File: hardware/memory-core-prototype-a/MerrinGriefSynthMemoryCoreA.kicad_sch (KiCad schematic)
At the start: 0 parts

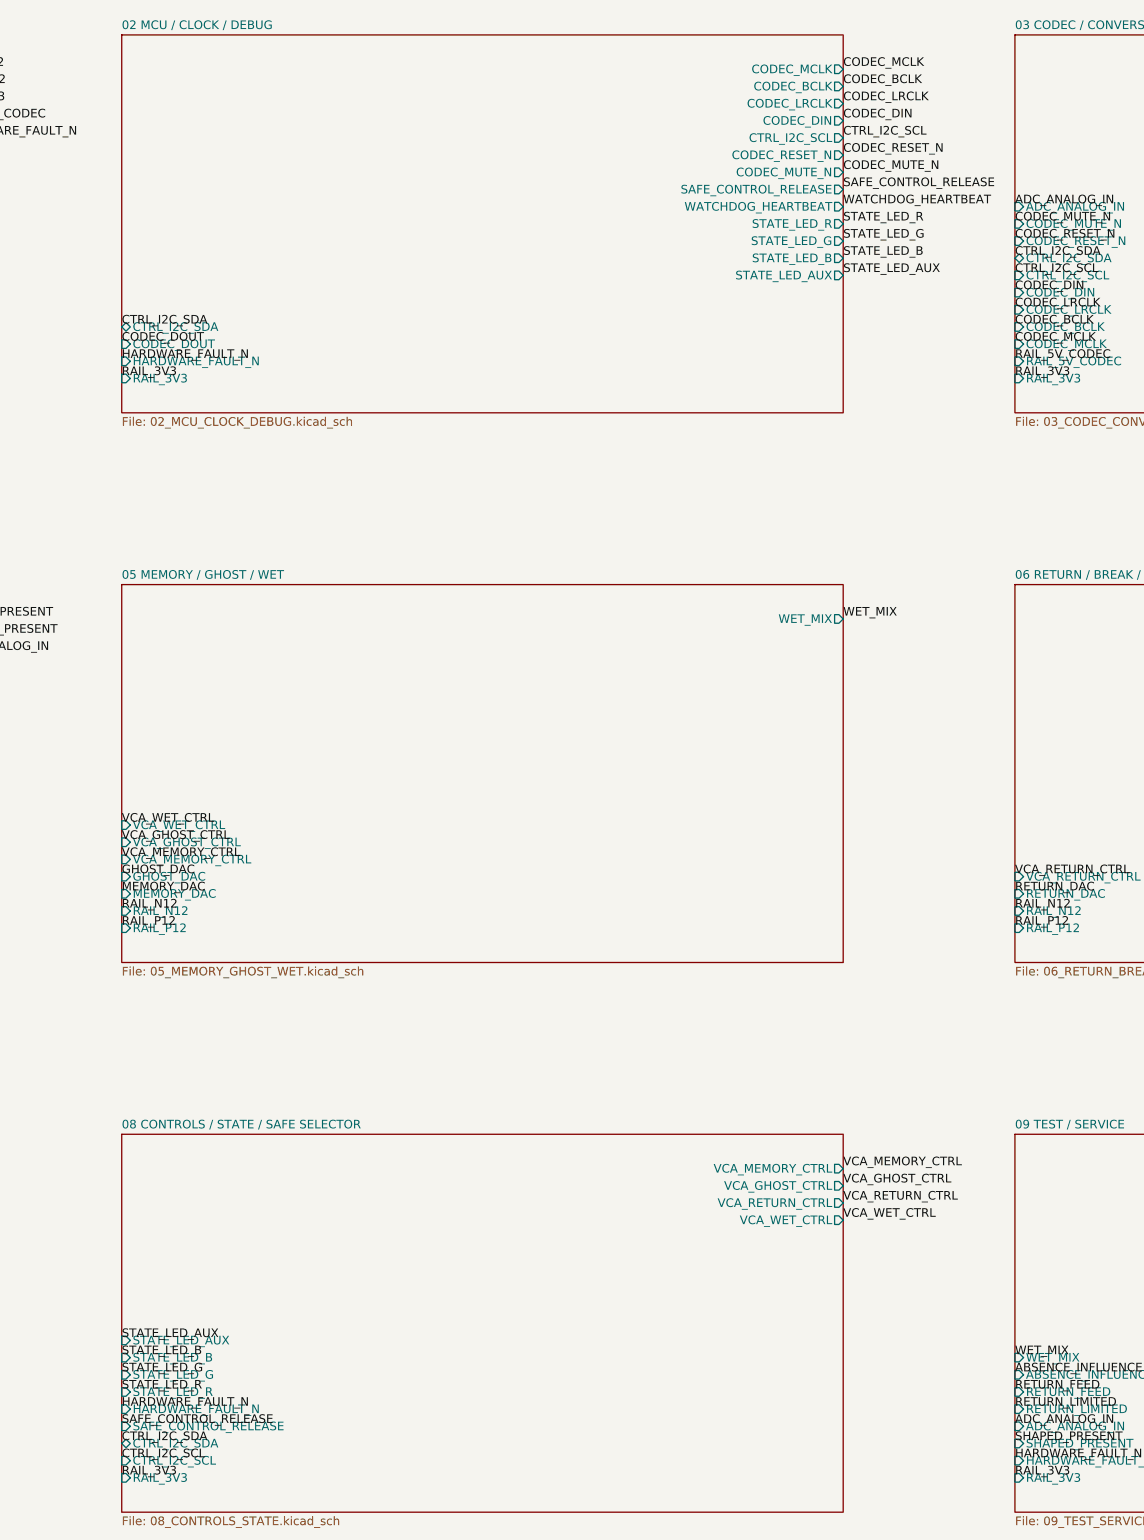
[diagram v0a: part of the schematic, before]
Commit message: Capture ERC-validated controls and state sheet
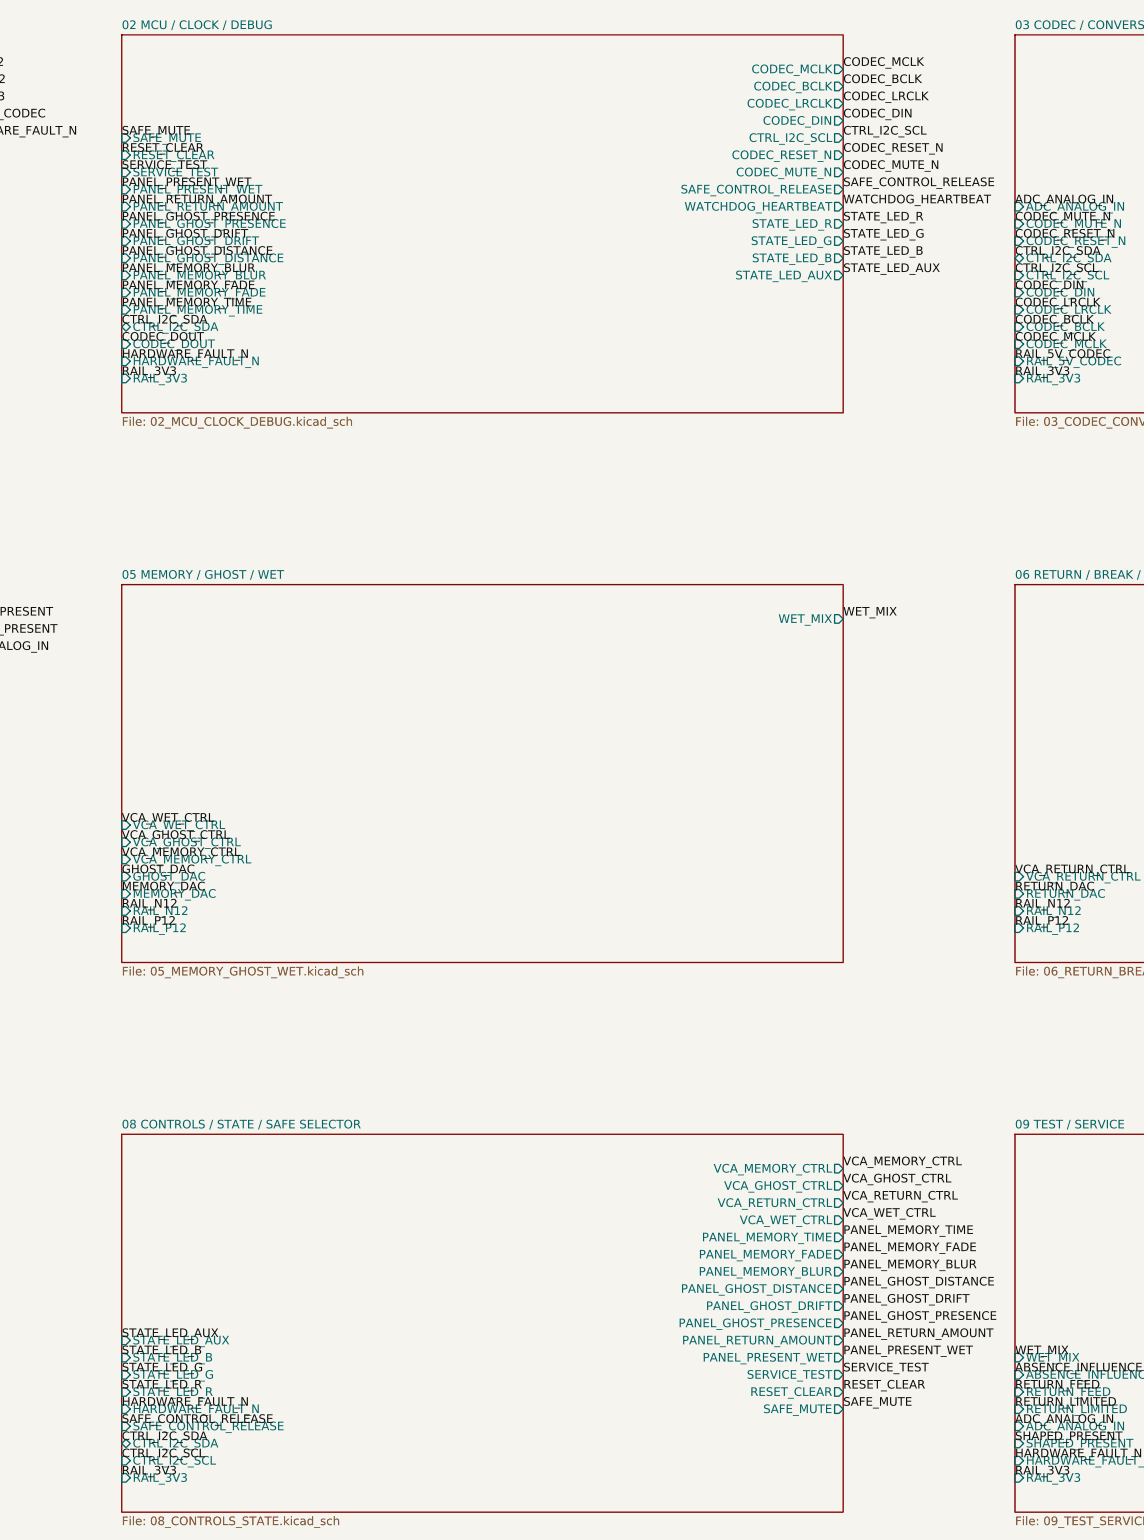
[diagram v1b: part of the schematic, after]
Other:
- sheet 02 MCU / CLOCK / DEBUG ports: added PANEL_GHOST_DISTANCE, PANEL_GHOST_DRIFT, PANEL_GHOST_PRESENCE, PANEL_MEMORY_BLUR, PANEL_MEMORY_FADE, PANEL_MEMORY_TIME, PANEL_PRESENT_WET, PANEL_RETURN_AMOUNT, RESET_CLEAR, SAFE_MUTE, SERVICE_TEST; removed none
- sheet 08 CONTROLS / STATE / SAFE SELECTOR ports: added PANEL_GHOST_DISTANCE, PANEL_GHOST_DRIFT, PANEL_GHOST_PRESENCE, PANEL_MEMORY_BLUR, PANEL_MEMORY_FADE, PANEL_MEMORY_TIME, PANEL_PRESENT_WET, PANEL_RETURN_AMOUNT, RESET_CLEAR, SAFE_MUTE, SERVICE_TEST; removed none

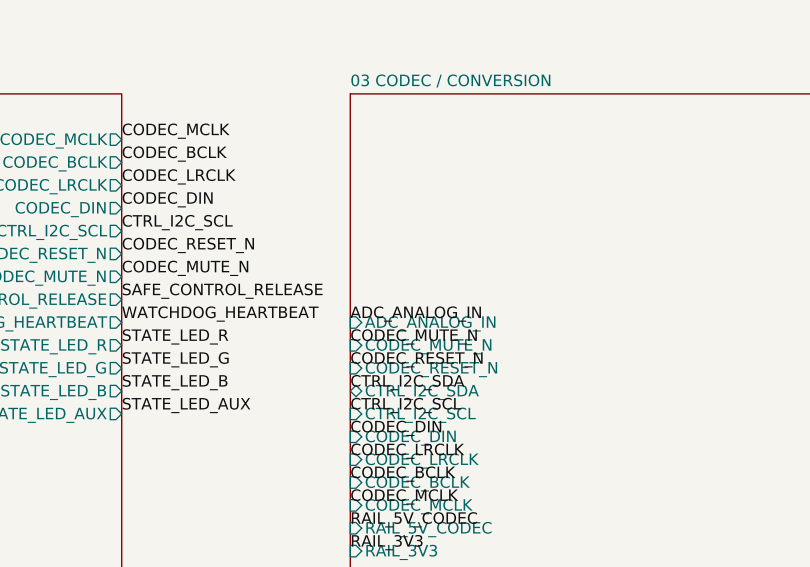
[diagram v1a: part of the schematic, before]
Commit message: Capture ERC-validated codec conversion sheet
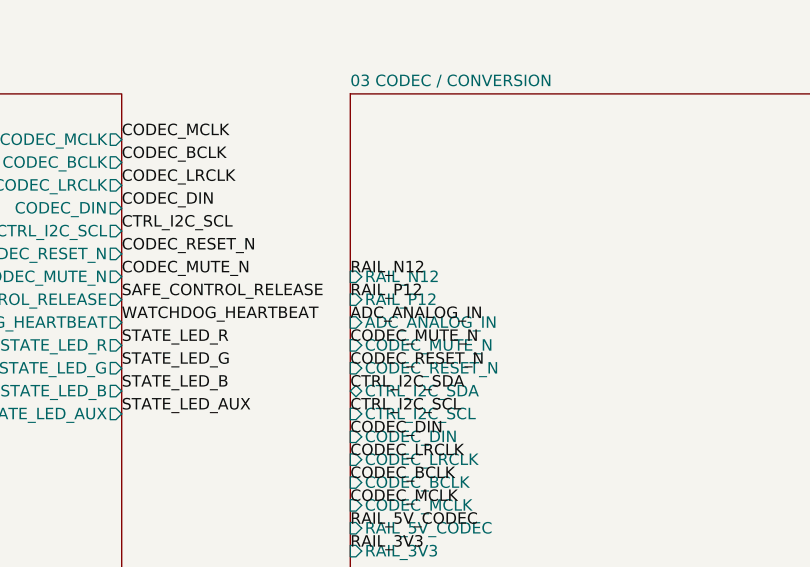
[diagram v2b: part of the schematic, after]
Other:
- sheet 03 CODEC / CONVERSION ports: added RAIL_N12, RAIL_P12; removed none
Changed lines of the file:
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@@
 	)
 	(label "PANEL_MEMORY_TIME"
-		(at 152.4 60.96 0)
+		(at 152.4 60.96 0.0000)
 		(effects
 			(font
@@
 	)
 	(label "PANEL_MEMORY_FADE"
-		(at 152.4 58.42 0)
+		(at 152.4 58.42 0.0000)
 		(effects
 			(font
@@
 	)
 	(label "PANEL_MEMORY_BLUR"
-		(at 152.4 55.88 0)
+		(at 152.4 55.88 0.0000)
 		(effects
 			(font
@@
 	)
 	(label "PANEL_GHOST_DISTANCE"
-		(at 152.4 53.34 0)
+		(at 152.4 53.34 0.0000)
 		(effects
 			(font
@@
 	)
 	(label "PANEL_GHOST_DRIFT"
-		(at 152.4 50.8 0)
+		(at 152.4 50.8 0.0000)
 		(effects
 			(font
@@
 	)
 	(label "PANEL_GHOST_PRESENCE"
-		(at 152.4 48.26 0)
+		(at 152.4 48.26 0.0000)
 		(effects
 			(font
@@
 	)
 	(label "PANEL_RETURN_AMOUNT"
-		(at 152.4 45.72 0)
+		(at 152.4 45.72 0.0000)
 		(effects
 			(font
@@
 	)
 	(label "PANEL_PRESENT_WET"
-		(at 152.4 43.18 0)
+		(at 152.4 43.18 0.0000)
 		(effects
 			(font
@@
 	)
 	(label "SERVICE_TEST"
-		(at 152.4 40.64 0)
+		(at 152.4 40.64 0.0000)
 		(effects
 			(font
@@
 	)
 	(label "RESET_CLEAR"
-		(at 152.4 38.1 0)
+		(at 152.4 38.1 0.0000)
 		(effects
 			(font
@@
 	)
 	(label "SAFE_MUTE"
-		(at 152.4 35.56 0)
+		(at 152.4 35.56 0.0000)
 		(effects
 			(font
@@
 	)
 	(label "PANEL_MEMORY_TIME"
-		(at 259.08 198.12 0)
+		(at 259.08 198.12 0.0000)
 		(effects
 			(font
@@
 	)
 	(label "PANEL_MEMORY_FADE"
-		(at 259.08 200.66 0)
+		(at 259.08 200.66 0.0000)
 		(effects
 			(font
@@
 	)
 	(label "PANEL_MEMORY_BLUR"
-		(at 259.08 203.2 0)
+		(at 259.08 203.2 0.0000)
 		(effects
 			(font
@@
 	)
 	(label "PANEL_GHOST_DISTANCE"
-		(at 259.08 205.74 0)
+		(at 259.08 205.74 0.0000)
 		(effects
 			(font
@@
 	)
 	(label "PANEL_GHOST_DRIFT"
-		(at 259.08 208.28 0)
+		(at 259.08 208.28 0.0000)
 		(effects
 			(font
@@
 	)
 	(label "PANEL_GHOST_PRESENCE"
-		(at 259.08 210.82 0)
+		(at 259.08 210.82 0.0000)
 		(effects
 			(font
@@
 	)
 	(label "PANEL_RETURN_AMOUNT"
-		(at 259.08 213.36 0)
+		(at 259.08 213.36 0.0000)
 		(effects
 			(font
@@
 	)
 	(label "PANEL_PRESENT_WET"
-		(at 259.08 215.9 0)
+		(at 259.08 215.9 0.0000)
 		(effects
 			(font
@@
 	)
 	(label "SERVICE_TEST"
-		(at 259.08 218.44 0)
+		(at 259.08 218.44 0.0000)
 		(effects
 			(font
@@
 	)
 	(label "RESET_CLEAR"
-		(at 259.08 220.98 0)
+		(at 259.08 220.98 0.0000)
 		(effects
 			(font
@@
 	)
 	(label "SAFE_MUTE"
-		(at 259.08 223.52 0)
+		(at 259.08 223.52 0.0000)
+		(effects
+			(font
+				(size 1.27 1.27)
+			)
+			(justify left bottom)
+		)
+	)
+	(label "RAIL_P12"
+		(at 284.48 43.18 0)
+		(effects
+			(font
+				(size 1.27 1.27)
+			)
+			(justify left bottom)
+		)
+	)
+	(label "RAIL_N12"
+		(at 284.48 40.64 0)
 		(effects
 			(font
@@
 			)
 		)
+		(pin "RAIL_P12" input
+			(at 284.48 43.18 180)
+			(effects
+				(font
+					(size 1.27 1.27)
+				)
+				(justify left)
+			)
+		)
+		(pin "RAIL_N12" input
+			(at 284.48 40.64 180)
+			(effects
+				(font
+					(size 1.27 1.27)
+				)
+				(justify left)
+			)
+		)
 		(instances
 			(project "MerrinGriefSynthMemoryCoreA"
@@
 		)
 		(pin "PANEL_MEMORY_TIME" output
-			(at 259.08 198.12 0)
+			(at 259.08 198.12 0.0000)
 			(effects
 				(font
@@
 		)
 		(pin "PANEL_MEMORY_FADE" output
-			(at 259.08 200.66 0)
+			(at 259.08 200.66 0.0000)
 			(effects
 				(font
@@
 		)
 		(pin "PANEL_MEMORY_BLUR" output
-			(at 259.08 203.2 0)
+			(at 259.08 203.2 0.0000)
 			(effects
 				(font
@@
 		)
 		(pin "PANEL_GHOST_DISTANCE" output
-			(at 259.08 205.74 0)
+			(at 259.08 205.74 0.0000)
 			(effects
 				(font
@@
 		)
 		(pin "PANEL_GHOST_DRIFT" output
-			(at 259.08 208.28 0)
+			(at 259.08 208.28 0.0000)
 			(effects
 				(font
@@
 		)
 		(pin "PANEL_GHOST_PRESENCE" output
-			(at 259.08 210.82 0)
+			(at 259.08 210.82 0.0000)
 			(effects
 				(font
@@
 		)
 		(pin "PANEL_RETURN_AMOUNT" output
-			(at 259.08 213.36 0)
+			(at 259.08 213.36 0.0000)
 			(effects
 				(font
@@
 		)
 		(pin "PANEL_PRESENT_WET" output
-			(at 259.08 215.9 0)
+			(at 259.08 215.9 0.0000)
 			(effects
 				(font
@@
 		)
 		(pin "SERVICE_TEST" output
-			(at 259.08 218.44 0)
+			(at 259.08 218.44 0.0000)
 			(effects
 				(font
@@
 		)
 		(pin "RESET_CLEAR" output
-			(at 259.08 220.98 0)
+			(at 259.08 220.98 0.0000)
 			(effects
 				(font
@@
 		)
 		(pin "SAFE_MUTE" output
-			(at 259.08 223.52 0)
-			(effects
-				(font
+			(at 259.08 223.52 0.0000)
+			(effects
+				(font

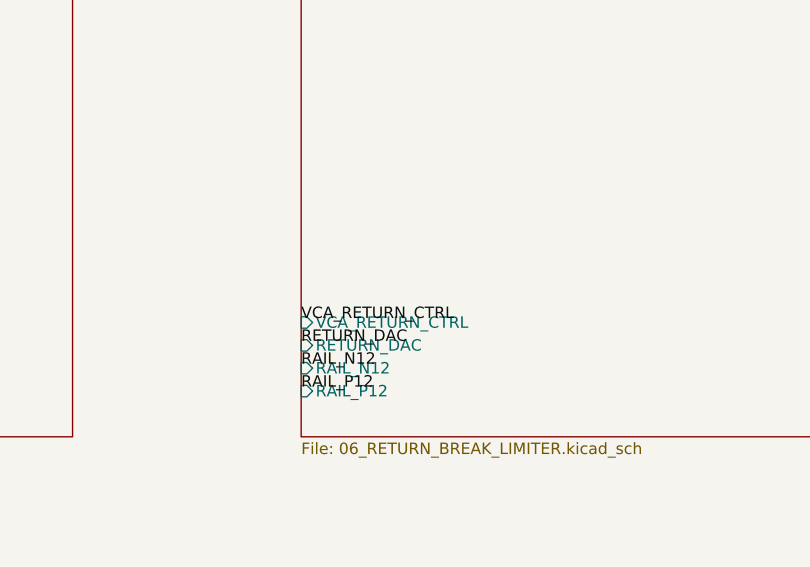
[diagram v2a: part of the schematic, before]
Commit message: Capture ERC-validated Return Break limiter sheet
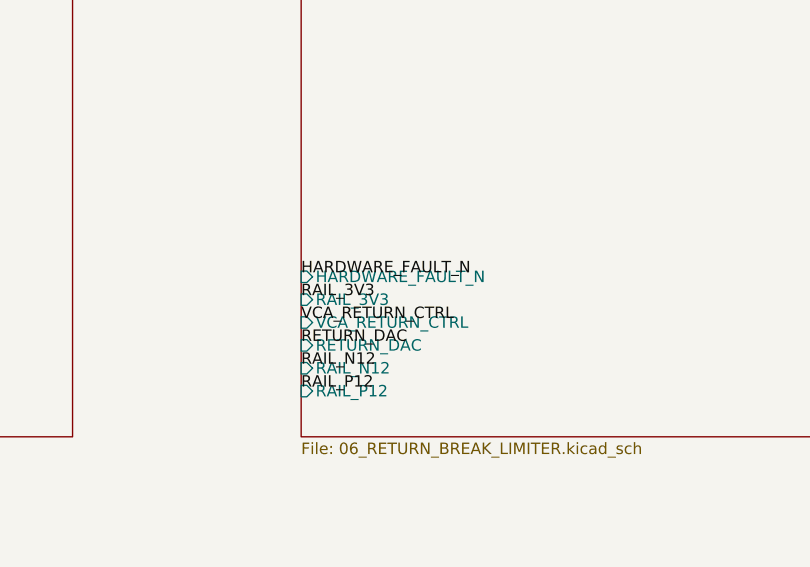
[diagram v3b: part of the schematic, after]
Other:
- sheet 06 RETURN / BREAK / LIMITER ports: added HARDWARE_FAULT_N, RAIL_3V3; removed none
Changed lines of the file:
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@@
 	)
 	(label "RAIL_P12"
-		(at 284.48 43.18 0)
+		(at 284.48 43.18 0.0000)
 		(effects
 			(font
@@
 	)
 	(label "RAIL_N12"
-		(at 284.48 40.64 0)
+		(at 284.48 40.64 0.0000)
+		(effects
+			(font
+				(size 1.27 1.27)
+			)
+			(justify left bottom)
+		)
+	)
+	(label "RAIL_3V3"
+		(at 284.48 142.24 0)
+		(effects
+			(font
+				(size 1.27 1.27)
+			)
+			(justify left bottom)
+		)
+	)
+	(label "HARDWARE_FAULT_N"
+		(at 284.48 139.7 0)
 		(effects
 			(font
@@
 			)
 		)
+		(pin "RAIL_3V3" input
+			(at 284.48 142.24 180)
+			(effects
+				(font
+					(size 1.27 1.27)
+				)
+				(justify left)
+			)
+		)
+		(pin "HARDWARE_FAULT_N" input
+			(at 284.48 139.7 180)
+			(effects
+				(font
+					(size 1.27 1.27)
+				)
+				(justify left)
+			)
+		)

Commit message: Complete final integrated schematic review
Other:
- note added: "All nine component sheets captured. Final integrated interface and ERC review."
- note removed: "Hierarchy/interface capture. Detailed circuits replace temporary harnesses sheet by sheet."
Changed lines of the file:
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@@
 	(title_block
 		(title "Merrin Grief Synth — Memory Core Prototype A")
-		(rev "V5.2 native hierarchy capture")
+		(rev "V5.2 integrated schematic review")
 		(company "MerrinLab")
 	)
@@
 		)
 	)
-	(text "Hierarchy/interface capture. Detailed circuits replace temporary harnesses sheet by sheet."
+	(text "All nine component sheets captured. Final integrated interface and ERC review."
 		(exclude_from_sim no)
 		(at 20.32 15.24 0.0000)
